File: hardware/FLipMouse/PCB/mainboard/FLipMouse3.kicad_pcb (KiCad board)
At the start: 2 copper layers, 61 x 32 mm, 81 parts, among them J1 SJ2-3574A, J2 SJ2-3574A, J3 M50-3900542, J4 Conn_ARM_JTAG_SWD_10, J5 Conn_02x05_Odd_Even, J6 USB_OTG, J7 Conn_01x06, Q1 BC847, Q2 BC847, Q3 BSH108, Q4 BSH108, Q5 BSH108, SW1 SW_Push, SW2 SW_Push, U1 ESP32-WROOM, U2 TSOP4838, U3 LPC11U24FBD, U4 TSR_1-2433, U5 MPXV7007GP, Y1 JA-12.000-18-DFE

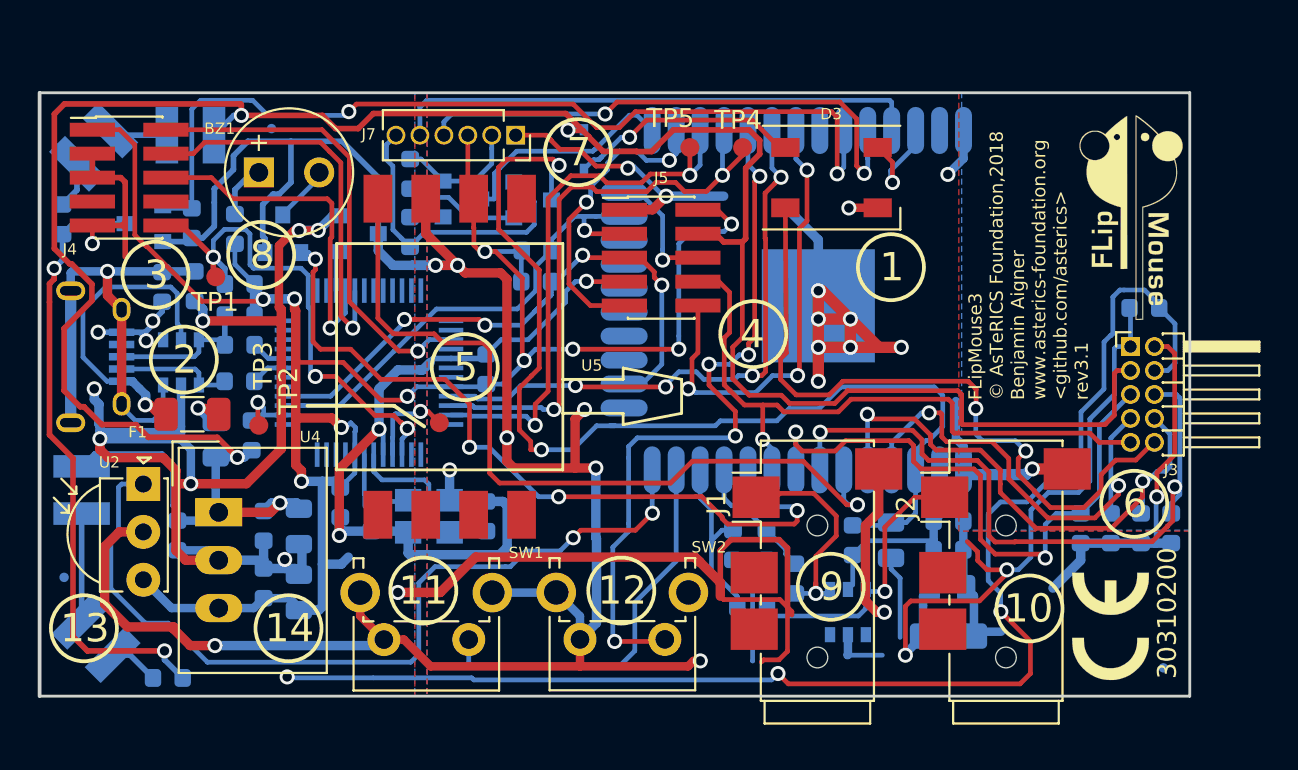
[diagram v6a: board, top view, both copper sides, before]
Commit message: Updated FLipMouse PCB: - Routed ADC inputs (FSR+pressure) to LPC11 too (in case of crappy ESP ADC values) - Added ESP32 auto-reset pins to LPC11 (enabling programming via LPC USB) - Cleanup regarding edge to trace spacing
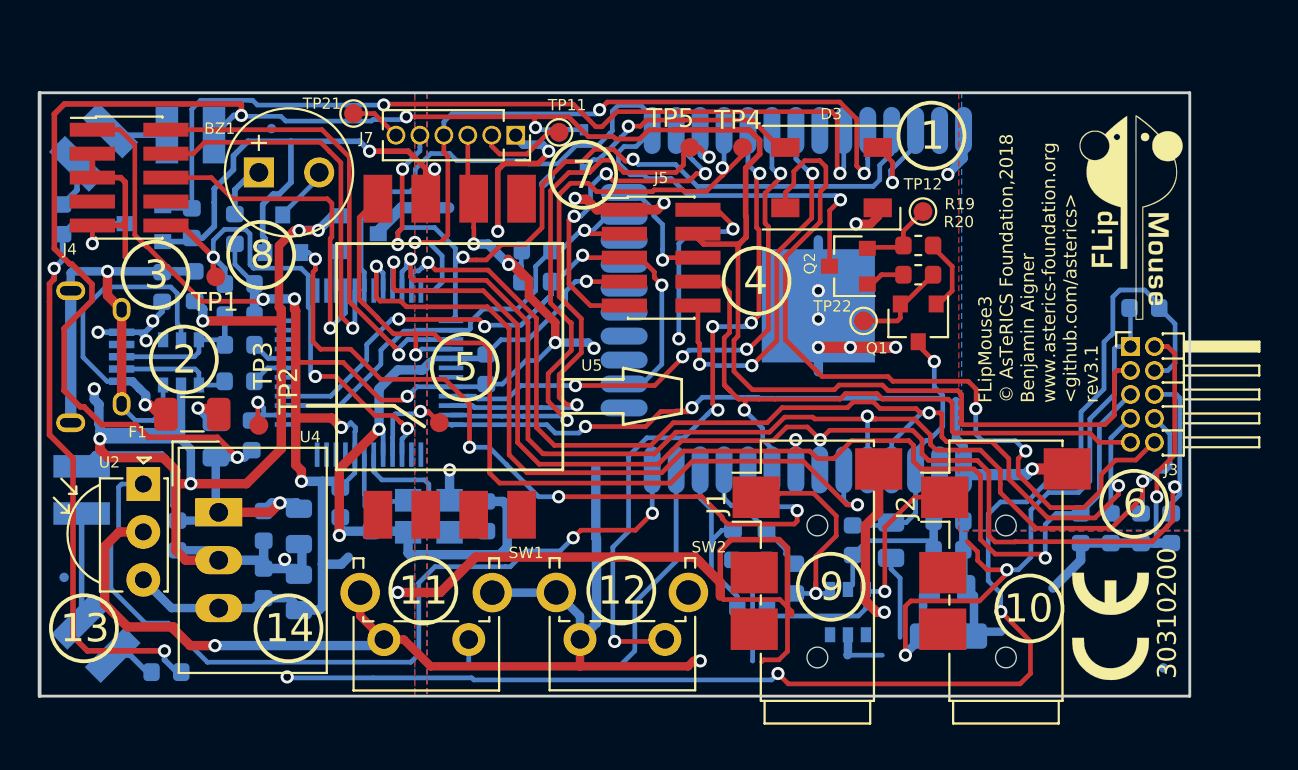
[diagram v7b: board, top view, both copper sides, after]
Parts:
- added TP11: TP, TestPoint:TestPoint_Pad_D1.0mm, F.Cu at (87.5, 120.1)
- added TP12: TP, TestPoint:TestPoint_Pad_D1.0mm, F.Cu at (106.8, 124.3)
- added TP21: TP, TestPoint:TestPoint_Pad_D1.0mm, F.Cu at (76.7, 119.1)
- added TP22: TP, TestPoint:TestPoint_Pad_D1.0mm, F.Cu at (103.7, 130.1)
- Q1, Q2, R19, R20: moved to F.Cu
- moved R19 27.2 mm to (106.6, 126.1), turned to 0 degrees
- moved R20 27.0 mm to (106.6, 127.7), turned to 180 degrees
- moved Q1 21.5 mm to (106.6, 130.2), turned to 270 degrees
- moved Q2 20.8 mm to (102.9, 127.2), turned to 180 degrees
- moved R1 0.32 mm to (66.7, 148.7)
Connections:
- Q1 pad 2: Net-(J7-Pad6) -> Net-(Q1-Pad2)
- Q2 pad 2: Net-(J7-Pad2) -> Net-(Q2-Pad2)
- R19 pad 1: Net-(J7-Pad2) -> Net-(Q2-Pad2)
- R20 pad 1: Net-(J7-Pad6) -> Net-(Q1-Pad2)
- U3 pad 30: (no net) -> /E_P0
- U3 pad 32: (no net) -> /FSR1
- U3 pad 33: (no net) -> /FSR2
- U3 pad 34: (no net) -> /FSR4
- U3 pad 35: (no net) -> /FSR3
- U3 pad 36: (no net) -> /U_TXD
- U3 pad 37: (no net) -> /U_RXD
- U3 pad 38: (no net) -> /SCL
- U3 pad 40: (no net) -> /PRESSURE
- U3 pad 48: (no net) -> /E_RESET
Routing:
- net GNDD: track 225.9 -> 186.8 mm, vias 21 -> 18
- net /FSR3: track 26.6 -> 63.8 mm, vias 2 -> 3
- net /FSR4: track 28.6 -> 64.3 mm, vias 2 -> 3
- net /FSR2: track 36.0 -> 70.3 mm, vias 2 -> 3
- net /FSR1: track 32.6 -> 65.8 mm, vias 2 -> 3
- net /E_P0: track 12.2 -> 43.6 mm, vias 0 -> 1
- net /U_RXD: track 28.2 -> 44.8 mm, vias 0 -> 4
- net /E_RESET: track 56.5 -> 41.1 mm, vias 2 -> 3
- net Net-(J7-Pad6): track 16.5 -> 2.73 mm
- net /U_TXD: track 29.2 -> 40.7 mm, vias 2 -> 3
- net +3V3: track 197.8 -> 192.2 mm, vias 13 -> 14
- net Net-(Q1-Pad2): track 0.00 -> 5.14 mm
- net /LED2: track 37.2 -> 42.2 mm
- net Net-(Q2-Pad2): track 0.00 -> 4.16 mm
- net /EXT_RX: track 24.4 -> 20.4 mm
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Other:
- net class Default: via_dia 0.8 -> 0.7; via_drill 0.5 -> 0.4

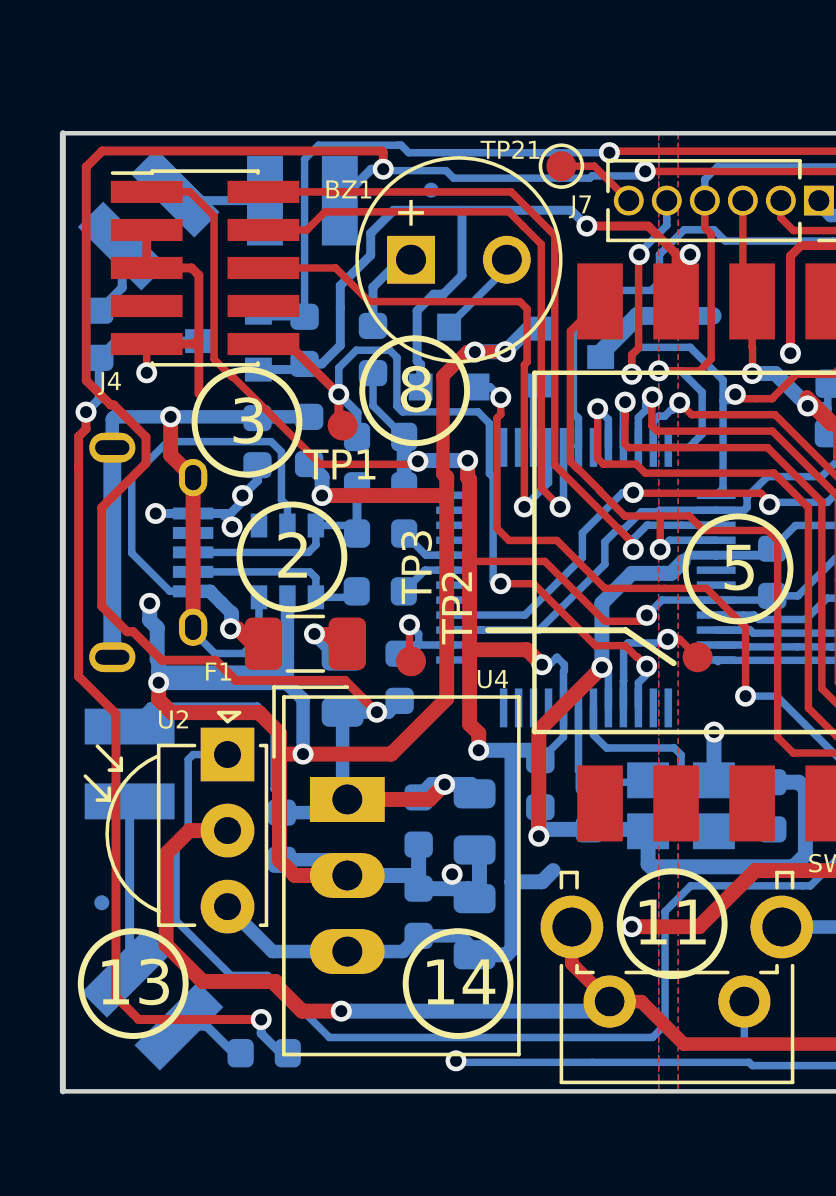
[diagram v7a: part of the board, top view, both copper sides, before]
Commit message: Small documentation updates. Fixed R10, according to batch documentation (batch 'a'), from 1k5 to 15R (series resistor for buzzer)
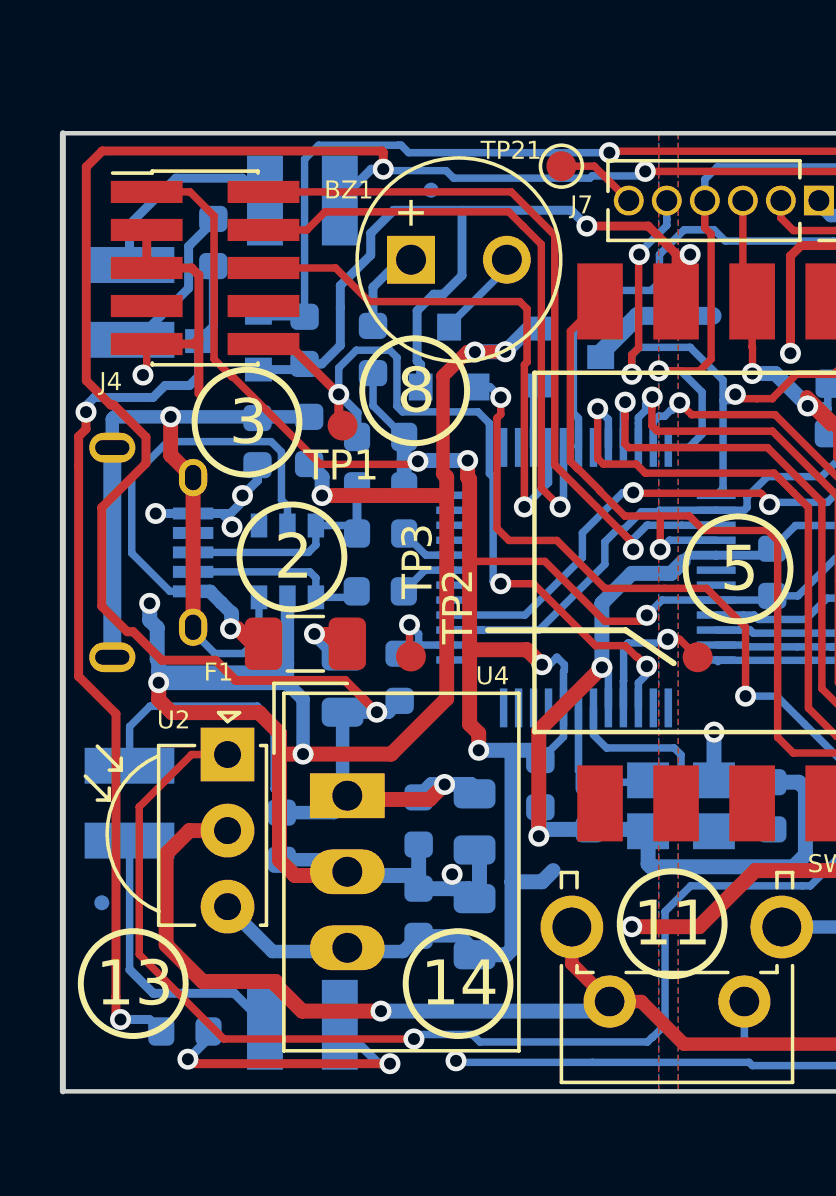
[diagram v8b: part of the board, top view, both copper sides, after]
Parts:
- moved D6 5.08 mm to (68.0, 147.8), turned to 180 degrees
- moved R2 4.89 mm to (65.0, 121.7)
- moved D7 2.84 mm to (62.2, 123.6), turned to 90 degrees
- moved R1 2.75 mm to (64.1, 148.0), turned to 180 degrees
- moved D4 1.31 mm to (62.2, 140.4)
- moved TP3 0.16 mm to (71.6, 135.5)
- moved U4 0.12 mm to (69.5, 140.1)
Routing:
- net Net-(D6-Pad1): track 2.64 -> 10.2 mm, vias 0 -> 2
- net Net-(D4-Pad1): track 5.79 -> 10.1 mm
- net Net-(D5-Pad1): track 3.10 -> 6.83 mm
- net Net-(D7-Pad1): track 2.48 -> 5.32 mm
- net /TSOP: track 45.9 -> 48.6 mm, vias 2 -> 3
- net Net-(Q4-Pad3): track 32.7 -> 30.7 mm
- net VBUS: track 135.8 -> 137.1 mm
